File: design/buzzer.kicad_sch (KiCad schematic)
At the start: 3 parts, among them J1 Conn_01x04_Pin, U6 ATtiny84A-M

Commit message: layout mostly done, schematic is done, need to generate new updated pdf
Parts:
- removed J1: Conn_01x04_Pin, symbol Connector:Conn_01x04_Pin
- added BZ1: CBT-09427-SMT-TR, footprints:CUI_CBT-09427-SMT, symbol Device:Buzzer
- added C11: 10uF, Capacitor_SMD:C_0402_1005Metric_Pad0.74x0.62mm_HandSolder, symbol Device:C_Small
- added C12: 100nF, Capacitor_SMD:C_0402_1005Metric_Pad0.74x0.62mm_HandSolder, symbol Device:C_Small
- added D66: D_Schottky, Diode_SMD:D_SOD-123, symbol Device:D_Schottky
- added JP1: SolderJumper_2_Bridged, Jumper:SolderJumper-2_P1.3mm_Bridged2Bar_RoundedPad1.0x1.5mm, symbol Jumper:SolderJumper_2_Bridged
- added Q3: MMBT3906, Package_TO_SOT_SMD:SOT-23, symbol Transistor_BJT:MMBT3906
- added Q4, Q5, Q6, Q7: BC848W, Package_TO_SOT_SMD:SOT-323_SC-70, symbol Transistor_BJT:BC848W
- added R11: USER, Resistor_SMD:R_0402_1005Metric_Pad0.72x0.64mm_HandSolder, symbol Device:R_Small
- added R12: 2.2k, Resistor_SMD:R_0402_1005Metric_Pad0.72x0.64mm_HandSolder, symbol Device:R_Small
- added R13, R15, R16, R17, R18, R9: 330, Resistor_SMD:R_0402_1005Metric_Pad0.72x0.64mm_HandSolder, symbol Device:R_Small
- added R14: 100, Resistor_SMD:R_0402_1005Metric_Pad0.72x0.64mm_HandSolder, symbol Device:R_Small
- renumbered R13 to R10, U6 to U5
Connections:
- net +3V3: now also Q3.2 (E)
- net GND: now also C11.2, C12.2, Q4.2 (E), Q5.2 (E), Q6.2 (E), Q7.2 (E)
- net VOL_0: now also U5.5 (AREF/PA0), R17.2; no longer U5.2 (PA3)
- net VOL_1: now also U5.4 (PA1), R18.1; no longer U5.3 (PA2)
- net VOL_2: now also U5.3 (PA2), R15.2; no longer U5.20 (PA5)
- net VOL_3: now also U5.2 (PA3), R16.2; no longer U5.15 (PA7)
- net SCK: now reaches U5.11 (XTAL1/PB0)
- net MISO: now reaches U5.12 (XTAL2/PB1)
- net MOSI: now reaches U5.14 (PB2)
- net RESET: now reaches U5.13 (~{RESET}/PB3)
- net RESET: now also R10.2
- net SCL renamed BUZZER_SCL
- net SDA renamed BUZZER_SDA
- removed net ~{RST}: R10.2, U5.4 (PA1)
- new net: Q5.1 (B), R16.1
- new net: Q5.3 (C), R11.1, R12.1
- new net: Q6.1 (B), R17.1
- new net: BZ1.M, D66.2 (A), JP1.2 (B), Q6.3 (C), R11.2, R13.2, R14.2
- new net: Q3.1 (B), R9.2
- new net: BZ1.P, D66.1 (K), Q3.3 (C)
- new net: Q4.1 (B), R15.1
- new net: Q7.1 (B), R18.2
- new net: Q4.3 (C), R13.1
- new net: Q7.3 (C), R14.1
- new net: JP1.1 (A), R12.2
- new net +3.3V: C11.1, C12.1
- new net ~{buzzer}: R9.1, U5.20 (PA5)
- new net ~{trigger}: U5.15 (PA7)
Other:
- note added: "0.5A 40V 460mV"
- note added: "Decoupling caps - place close to U6"
- note added: "Pins 11,12,13, and 14 are used for programming"
- note added: "Programming Pins"
- note added: "cut trace to use user chosen resistor"
- note removed: "Spare IO"
- moved on the sheet: R10, U5

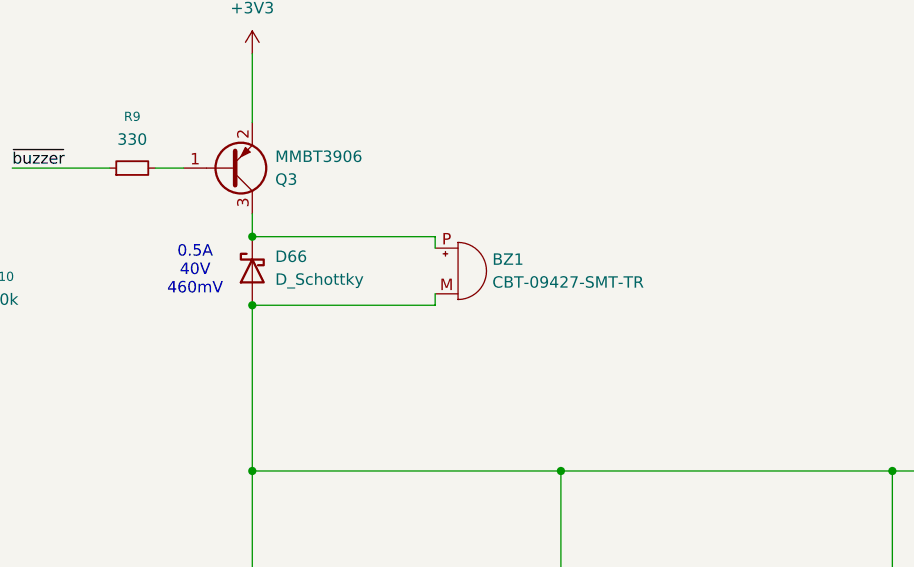
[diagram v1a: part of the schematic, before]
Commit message: Layout and Schematic Done
Almost ready for first release with tag. DRC etc passing, DFM checks pass on JLCPCB, but I need to go through sourcing components and ensure we have them all available before pushing the button on the orders
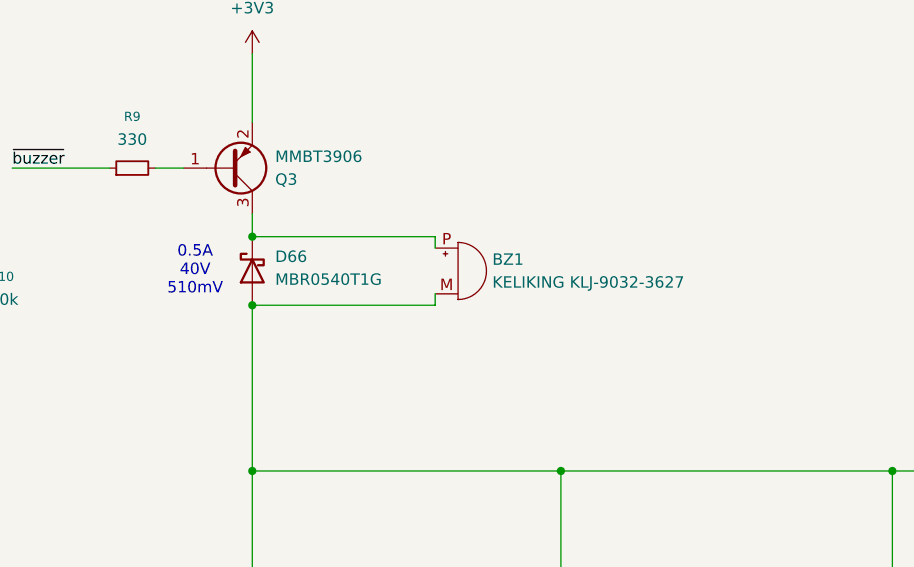
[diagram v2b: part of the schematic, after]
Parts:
- BZ1: value CBT-09427-SMT-TR -> KELIKING KLJ-9032-3627
- D66: value D_Schottky -> MBR0540T1G
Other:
- note added: "0.5A 40V 510mV"
- note removed: "0.5A 40V 460mV"
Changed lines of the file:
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@@
 		)
 	)
-	(text "0.5A\n40V\n460mV"
+	(text "0.5A\n40V\n510mV"
 		(exclude_from_sim no)
 		(at 140.97 69.85 0)
@@
 			)
 		)
-		(property "Value" "CBT-09427-SMT-TR"
+		(property "Value" "KELIKING KLJ-9032-3627"
 			(at 173.99 71.1199 0)
 			(effects
@@
 			)
 		)
-		(property "Value" "D_Schottky"
+		(property "Value" "MBR0540T1G"
 			(at 149.86 70.8024 90)
 			(effects
